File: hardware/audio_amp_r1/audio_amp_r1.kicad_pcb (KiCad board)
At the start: 2 copper layers, 100 x 50 mm, 15 parts, among them J1 AudioJack4, J2 AudioJack4, J3 Conn_01x02, J4 Conn_01x04_Pin, J5 Conn_01x04_Pin, U1 AD8397

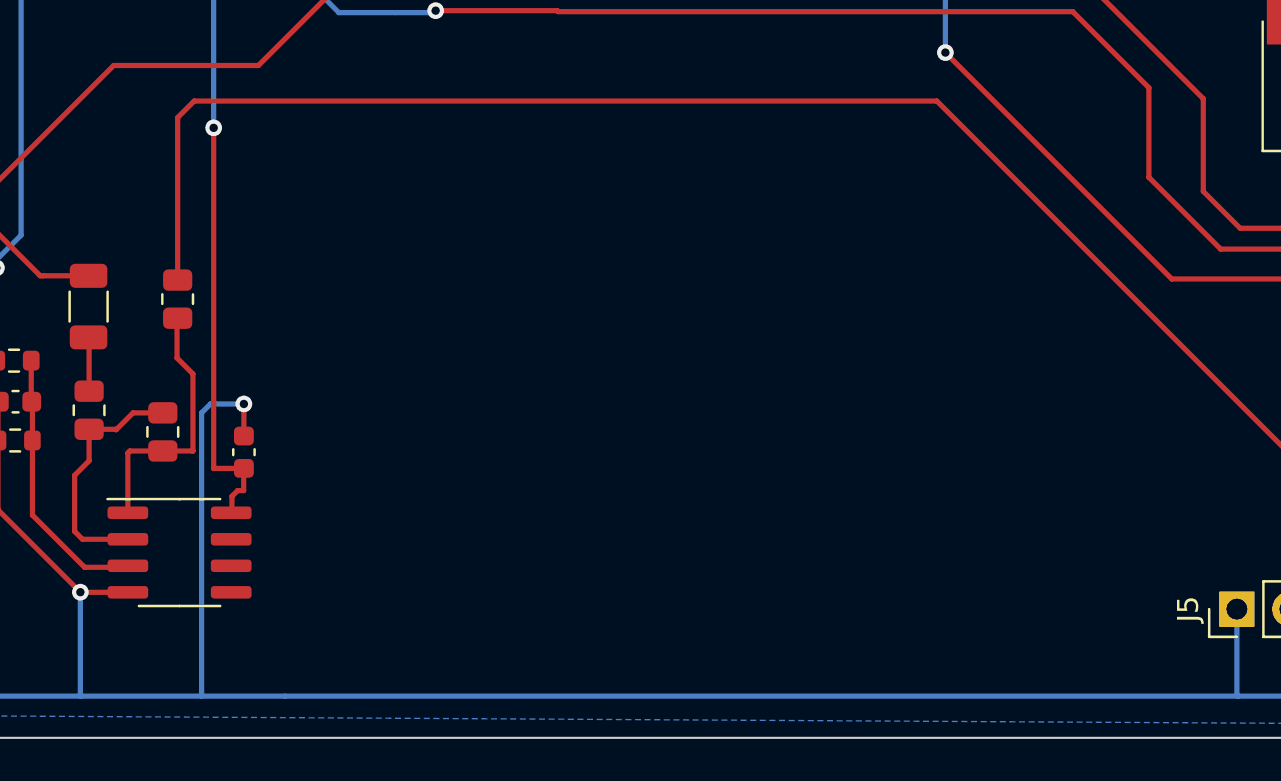
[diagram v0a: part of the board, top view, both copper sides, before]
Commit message: start updates for BNC connectors
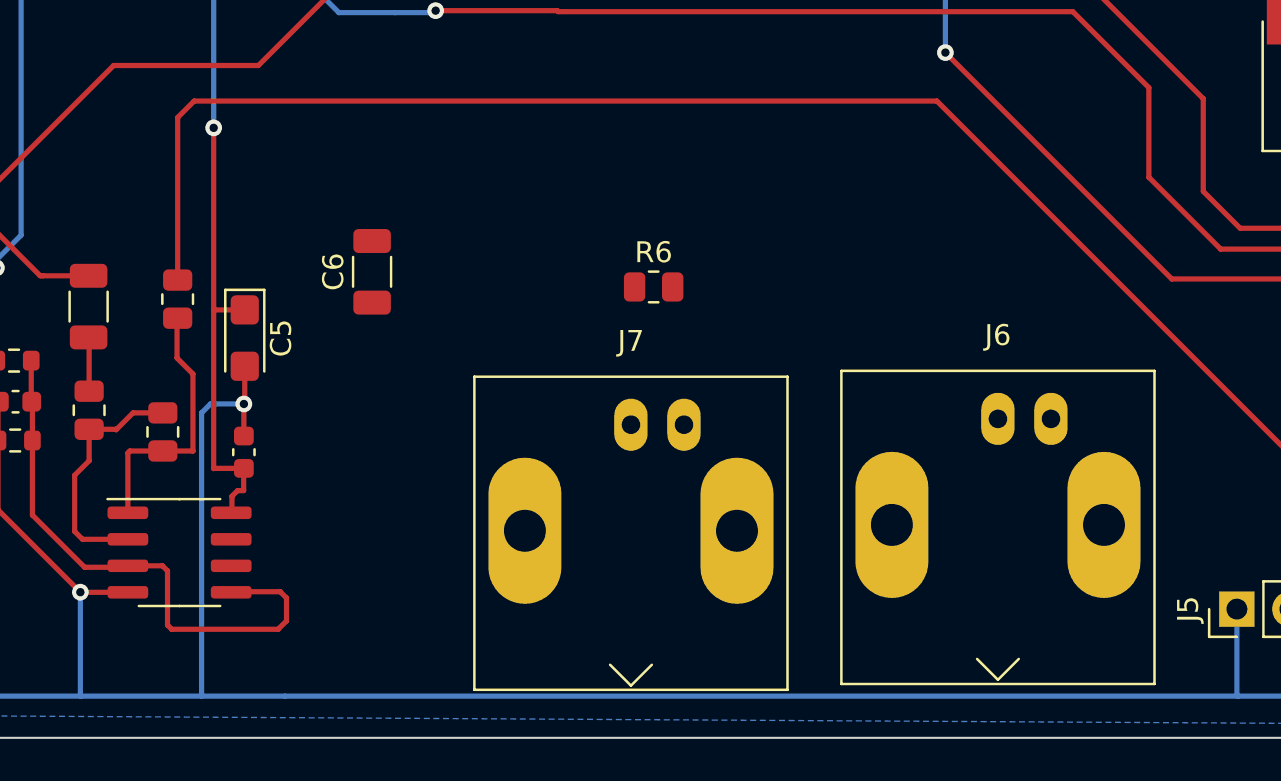
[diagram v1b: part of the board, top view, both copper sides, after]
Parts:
- added C5: 10uF, Capacitor_Tantalum_SMD:CP_EIA-3216-12_Kemet-S, F.Cu at (135.9, 80.8)
- added C6: 10uF, Capacitor_SMD:C_1206_3216Metric, F.Cu at (142.0, 77.7)
- added J6: KH-BNC50-3511, Connector_Coaxial:BNC_Amphenol_B6252HB-NPP3G-50_Horizontal, F.Cu at (172.0, 84.7)
- added J7: KH-BNC50-3511, Connector_Coaxial:BNC_Amphenol_B6252HB-NPP3G-50_Horizontal, F.Cu at (154.4, 85.0)
- added R6: 600R, Resistor_SMD:R_0805_2012Metric, F.Cu at (155.5, 78.4)
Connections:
- J5 pad 2: unconnected-(J5-Pin_2-Pad2) -> Net-(J5-Pin_2)
- R4 pad 1: Net-(R4-Pad1) -> Net-(J5-Pin_3)
- R5 pad 1: Net-(J5-Pin_3) -> Net-(J6-In)
- R5 pad 2: Net-(R4-Pad1) -> Net-(J5-Pin_3)
- U1 pad 1: Net-(R4-Pad1) -> Net-(J5-Pin_3)
- U1 pad 5: unconnected-(U1B-+-Pad5) -> Net-(U1A-+)
- U1 pad 7: unconnected-(U1-Pad7) -> Net-(J5-Pin_2)
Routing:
- net Net-(U1A-+): track 13.1 -> 27.5 mm
- net Net-(R4-Pad1): track 12.7 -> 0.00 mm
- net Net-(J5-Pin_3): track 76.9 -> 89.6 mm
- net GND: track 235.3 -> 237.1 mm
- net +3.3V: track 173.0 -> 174.5 mm

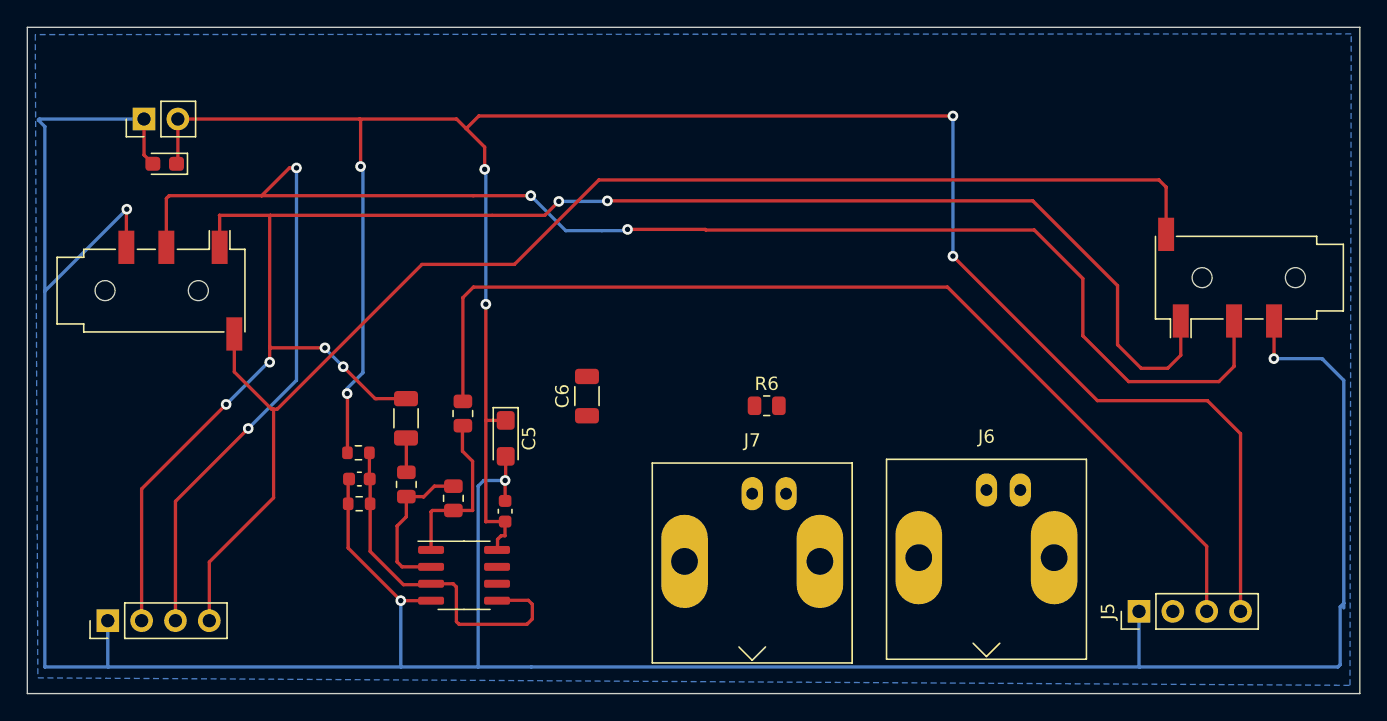
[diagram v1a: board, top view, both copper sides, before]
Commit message: update parts numbers and footprints
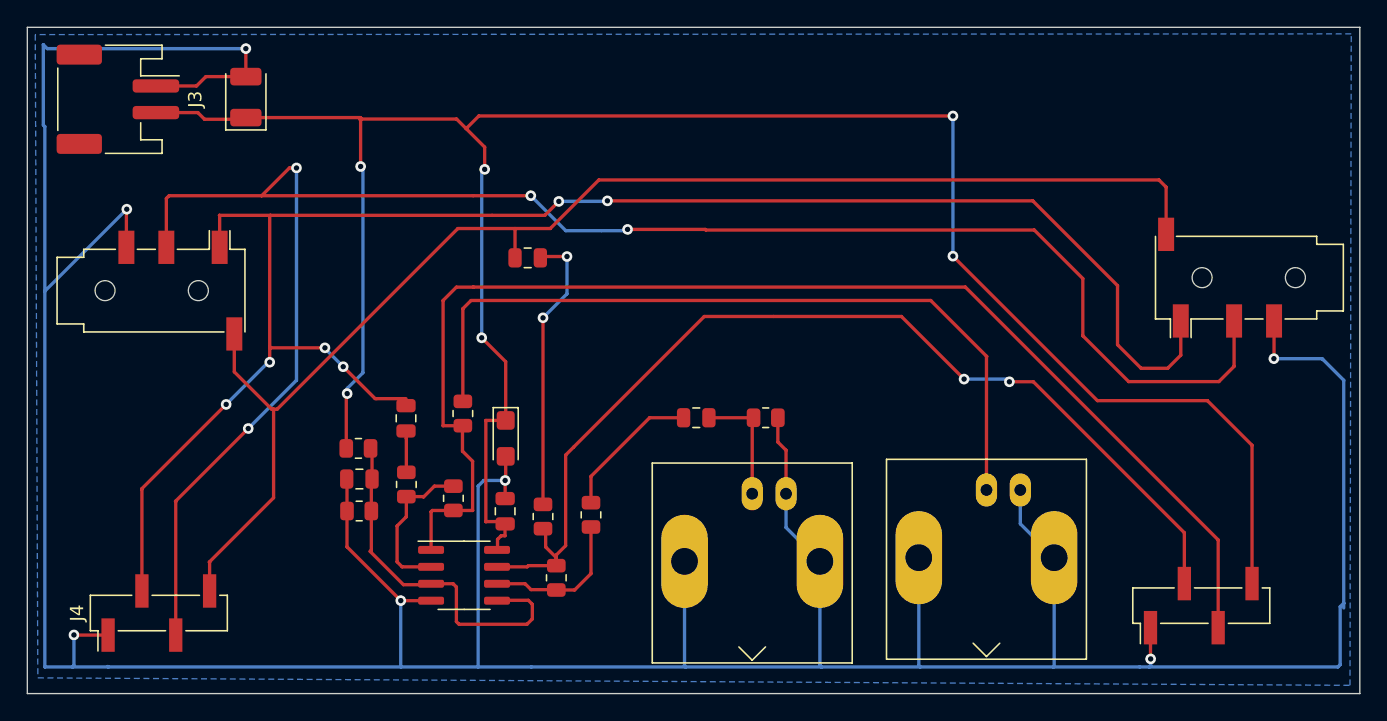
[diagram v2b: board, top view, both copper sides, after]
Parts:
- added C7: 10uF, Capacitor_SMD:C_0805_2012Metric, F.Cu at (150.2, 79.3)
- added R7: 10K, Resistor_SMD:R_0805_2012Metric, F.Cu at (142.3, 86.6)
- added R8: 10K, Resistor_SMD:R_0805_2012Metric, F.Cu at (139.7, 91.3)
- added R9: 560R, Resistor_SMD:R_0805_2012Metric, F.Cu at (138.7, 86.7)
- C1, C3: footprint Capacitor_SMD:C_0603_1608Metric -> Capacitor_SMD:C_0805_2012Metric
- C2, C6: footprint Capacitor_SMD:C_1206_3216Metric -> Capacitor_SMD:C_0805_2012Metric
- C4: value C_Polarized -> 100uF; footprint Capacitor_Tantalum_SMD:CP_EIA-2012-12_Kemet-R -> Capacitor_Tantalum_SMD:CP_EIA-3528-21_Kemet-B
- C5: footprint Capacitor_Tantalum_SMD:CP_EIA-3216-12_Kemet-S -> Capacitor_Tantalum_SMD:CP_EIA-3216-18_Kemet-A
- J1, J2: value AudioJack4 -> PJ-320D
- J3: value Conn_01x02 -> JST_PH_1x02; footprint Connector_PinHeader_2.54mm:PinHeader_1x02_P2.54mm_Vertical -> Connector_JST:JST_PH_S2B-PH-SM4-TB_1x02-1MP_P2.00mm_Horizontal
- J4, J5: footprint Connector_PinHeader_2.54mm:PinHeader_1x04_P2.54mm_Vertical -> Connector_PinHeader_2.54mm:PinHeader_1x04_P2.54mm_Vertical_SMD_Pin1Left
- R1, R2: footprint Resistor_SMD:R_0603_1608Metric -> Resistor_SMD:R_0805_2012Metric
- R5, R6: value 600R -> 560R
- moved C6 11.3 mm to (137.6, 67.3), turned to 180 degrees
- moved C4 7.88 mm to (116.4, 55.2), turned to 90 degrees
- moved J5 4.69 mm to (188.1, 93.4)
- moved J4 3.87 mm to (109.9, 94.0)
- moved J3 2.46 mm to (106.8, 55.4), turned to -90 degrees
- moved R6 0.90 mm to (155.4, 79.3)
- moved R2 0.54 mm to (124.9, 86.3)
- moved R1 0.33 mm to (124.8, 81.6)
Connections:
- C6 pad 1: unconnected-(C6-Pad1) -> Net-(C6-Pad1)
- U1 pad 6: unconnected-(U1B---Pad6) -> Net-(U1B--)
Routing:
- net Net-(J5-Pin_2): track 0.00 -> 77.5 mm, vias 0 -> 2
- net GND: track 237.1 -> 306.5 mm, vias 4 -> 7
- net Net-(J6-In): track 0.00 -> 58.3 mm
- net Net-(C6-Pad1): track 0.00 -> 21.4 mm, vias 0 -> 2
- net Net-(U1B--): track 0.00 -> 11.3 mm
- net Net-(C7-Pad2): track 0.00 -> 10.7 mm
- net Net-(J7-In): track 0.00 -> 9.09 mm
- net Net-(J5-Pin_3): track 89.6 -> 96.6 mm
- net +3.3V: track 174.5 -> 171.9 mm
- net /Left: track 132.1 -> 129.9 mm
- net /Right: track 137.4 -> 138.4 mm

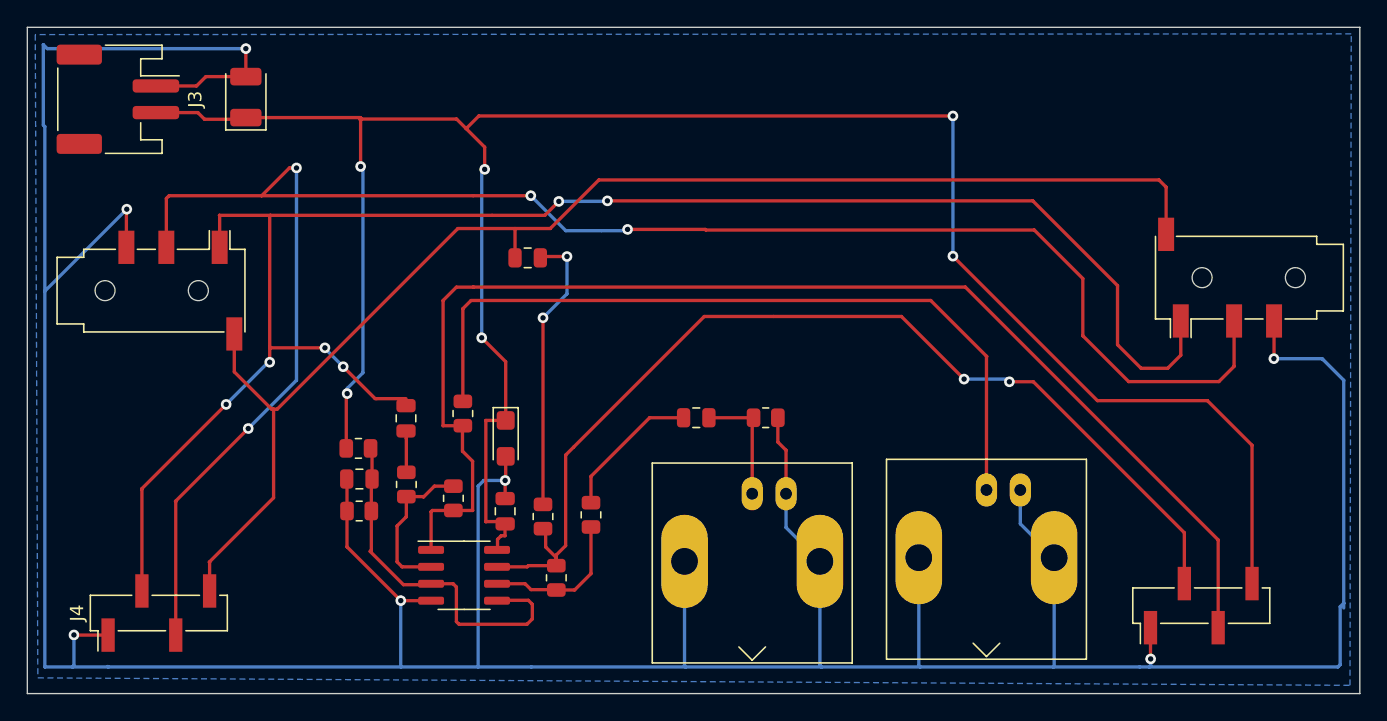
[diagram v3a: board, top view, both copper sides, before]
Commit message: update circuit to drive mic
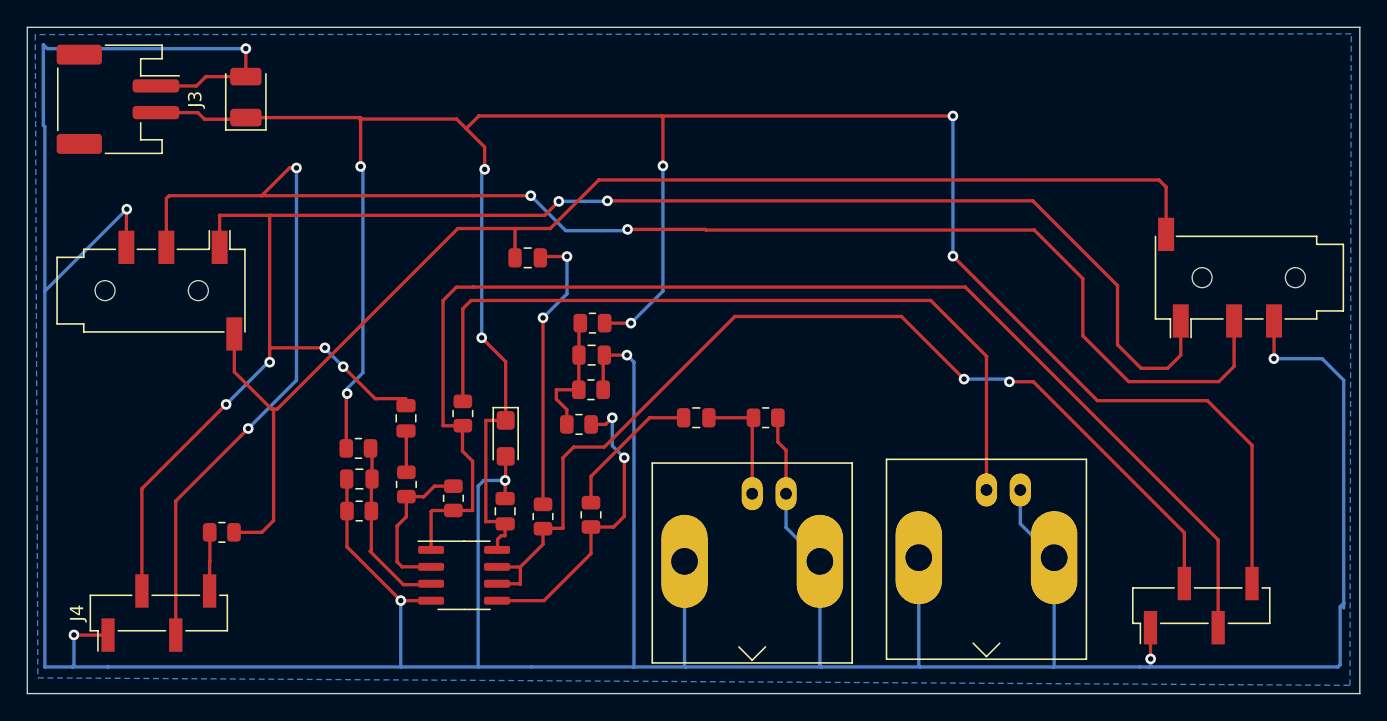
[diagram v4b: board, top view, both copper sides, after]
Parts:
- added C8: 0.1uF, Capacitor_SMD:C_0805_2012Metric, F.Cu at (142.3, 74.6)
- added R10: 1K5, Resistor_SMD:R_0805_2012Metric, F.Cu at (114.6, 87.9)
- added R11: 47k, Resistor_SMD:R_0805_2012Metric, F.Cu at (142.3, 77.2)
- added R12: 100R, Resistor_SMD:R_0805_2012Metric, F.Cu at (141.4, 79.8)
- R3: value 10K -> 1K
- R4: value 100K -> 20K
- R8: value 10K -> 47k
- moved R8 19.3 mm to (142.4, 72.2), turned to 0 degrees
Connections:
- J4 pad 4: /Mic -> Net-(J4-Pin_4)
- R7 pad 2: Net-(U1B--) -> Net-(U1B-+)
- R8 pad 1: Net-(U1B--) -> Net-(C8-Pad2)
- R8 pad 2: Net-(J5-Pin_2) -> +3.3V
- U1 pad 5: Net-(U1A-+) -> Net-(U1B-+)
- U1 pad 6: Net-(U1B--) -> Net-(J5-Pin_2)
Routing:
- net GND: track 306.5 -> 334.4 mm, vias 7 -> 8
- net Net-(U1B-+): track 0.00 -> 22.9 mm, vias 0 -> 2
- net +3.3V: track 171.9 -> 190.5 mm, vias 6 -> 8
- net Net-(U1A-+): track 27.8 -> 13.4 mm
- net Net-(U1B--): track 11.3 -> 0.00 mm
- net Net-(C8-Pad2): track 0.00 -> 9.66 mm
- net Net-(J4-Pin_4): track 0.00 -> 4.36 mm
- net /Mic: track 102.7 -> 98.7 mm
- net Net-(J5-Pin_2): track 77.5 -> 76.7 mm

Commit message: update prod files
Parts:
- added J8: Conn_01x04_Pin, Connector_PinHeader_2.54mm:PinHeader_1x04_P2.54mm_Vertical_SMD_Pin1Left, F.Cu at (130.1, 94.4)
- R4: value 20K -> 22K
- moved R3 4.17 mm to (127.1, 80.4)
- moved R5 4.17 mm to (131.3, 75.1)
- moved U1 4.17 mm to (131.4, 87.2)
- moved C2 4.17 mm to (127.0, 75.4)
- moved C3 4.17 mm to (123.5, 80.0)
- moved R1 4.17 mm to (123.5, 77.7)
- moved R2 4.17 mm to (123.5, 82.4)
- moved C1 4.17 mm to (134.5, 82.4)
- moved C5 4.17 mm to (134.5, 76.9)
- moved R4 4.17 mm to (130.6, 81.4)
- moved R9 3.32 mm to (139.6, 83.5)
- moved J6 0.60 mm to (172.0, 85.3)
- moved J7 0.30 mm to (154.4, 85.3)
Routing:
- net +3.3V: track 190.5 -> 209.9 mm, vias 8 -> 5
- net Net-(J8-Pin_4): track 9.66 -> 27.8 mm, vias 0 -> 2
- net Net-(J8-Pin_1): track 11.8 -> 26.2 mm, vias 0 -> 2
- net Net-(J8-Pin_3): track 22.9 -> 33.3 mm
- net Net-(J5-Pin_3): track 96.6 -> 104.9 mm
- net GND: track 334.4 -> 342.4 mm
- net Net-(J5-Pin_2): track 76.7 -> 72.9 mm
- net Net-(J6-In): track 58.3 -> 54.9 mm
- net /Left: track 129.9 -> 131.0 mm
- net /Mic: track 98.7 -> 99.5 mm
- net Net-(C6-Pad1): track 21.4 -> 20.8 mm

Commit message: update with tool holes and labels
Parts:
- added H1: JLCPCB-Tool-Hole, FootprintLib:MountingHole_JLCPCB_Tool, F.Cu at (196.7, 52.8)
- added H2: JLCPCB-Tool-Hole, FootprintLib:MountingHole_JLCPCB_Tool, F.Cu at (103.8, 94.0)
- added H3: JLCPCB-Tool-Hole, FootprintLib:MountingHole_JLCPCB_Tool, F.Cu at (196.6, 96.8)
- moved R10 2.70 mm to (117.3, 88.0)
- moved J4 2.70 mm to (112.6, 94.1)
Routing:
- net GND: track 342.4 -> 338.8 mm
- net /Mic: track 99.5 -> 97.3 mm
- net /Left: track 131.0 -> 130.0 mm
- net /Right: track 138.4 -> 137.4 mm
- net +3.3V: track 209.9 -> 210.8 mm
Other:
- board text added: "Audio Test Rev A Cullen Jennings Aug 2023"
- board text added: "JLCJLCJLCJLC"

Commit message: update prod
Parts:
- J1, J2: footprint Connector_Audio:Jack_3.5mm_PJ320D_Horizontal -> FootprintLib:Jack_3.5mm_PJ320D_Horizontal-CJ
- moved J1 1.41 mm to (109.2, 69.8)
- moved J2 1.30 mm to (191.7, 68.8)

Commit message: sent to prod
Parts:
- J6, J7: footprint Connector_Coaxial:BNC_Amphenol_B6252HB-NPP3G-50_Horizontal -> FootprintLib:BNC_Amphenol_B6252HB-NPP3G-50_Horizontal-CJ
- moved J1 80.4 mm to (189.6, 68.8), turned to 180 degrees
- moved J2 80.4 mm to (111.3, 69.7), turned to 0 degrees
- moved J6 2.58 mm to (172.0, 87.9)
- moved J7 2.42 mm to (154.4, 87.7)
